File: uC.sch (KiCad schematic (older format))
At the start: 23 parts, among them J4 SWD, SW2 RESET, SW3 BOOT, U9 STM32L073CZTx, Y1 8MHz, Y2 32.768kHz

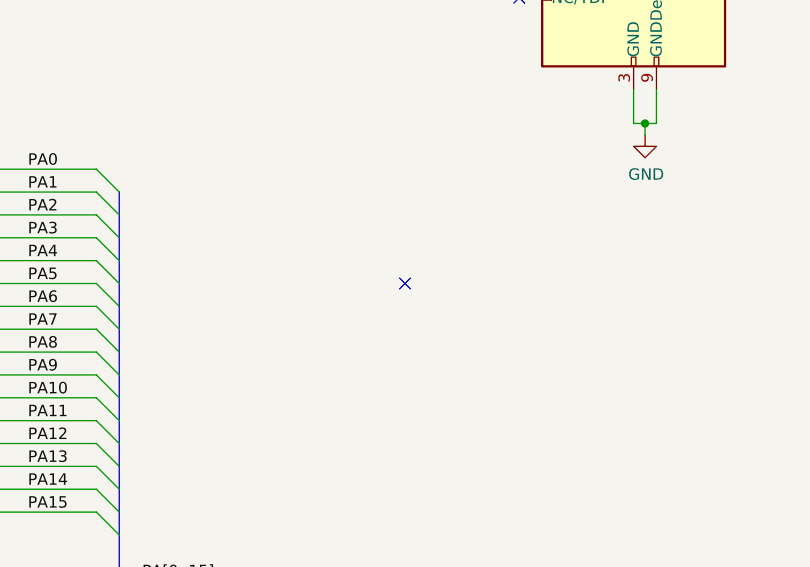
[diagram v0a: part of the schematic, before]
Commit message: Add digikey pn's to schematic, update BOM
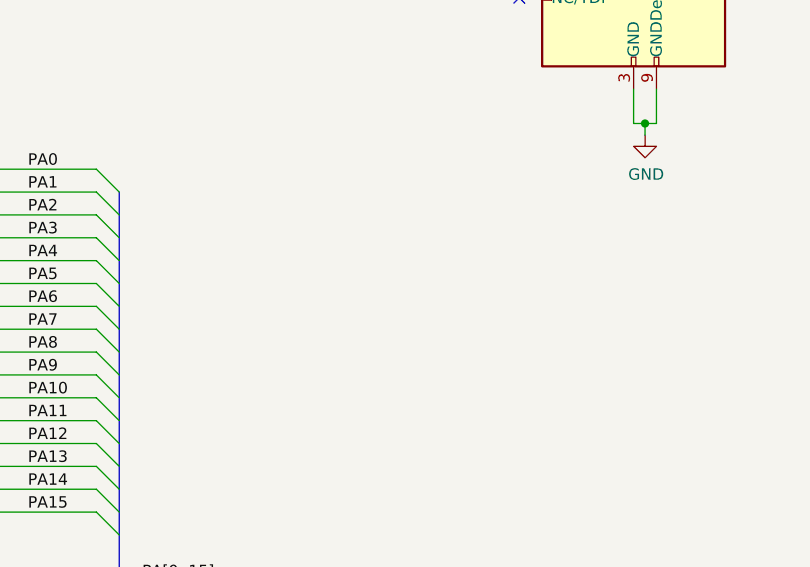
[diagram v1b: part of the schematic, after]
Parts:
- C18, C19, C20, C25, C28: Digikey (none) -> 490-14603-1-ND
- C21, C23, L4: Digikey (none) -> 587-1932-1-ND
- C22: Digikey (none) -> 311-1439-1-ND
- C24, C26: Digikey (none) -> 311-1666-1-ND
- C27, C29: Digikey (none) -> 311-1017-1-ND
- J4: Digikey (none) -> SAM8796-ND; LCSC (none) -> DNP
- R13, R14: Digikey (none) -> 311-10.0KLRTR-ND
- R15: Digikey (none) -> 311-330LRCT-ND
- SW2, SW3: Digikey (none) -> EG2531CT-ND
- U9: Digikey (none) -> 497-17506-ND; LCSC (none) -> DNP
- Y1: Digikey (none) -> 535-10630-1-ND
- Y2: Digikey (none) -> 535-9542-1-ND
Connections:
- no-connect marks 3 -> 2
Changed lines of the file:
@@
 F 2 "jlcpcb_smt:LQFP-48_7x7mm_P0.5mm" H 5800 2850 50  0001 R CNN
 F 3 "http://www.st.com/st-web-ui/static/active/en/resource/technical/document/datasheet/DM00141036.pdf" H 6400 4250 50  0001 C CNN
-F 4 "" H 6400 4250 50  0001 C CNN "LCSC"
+F 4 "DNP" H 6400 4250 50  0001 C CNN "LCSC"
+F 5 "497-17506-ND" H 6400 4250 50  0001 C CNN "Digikey"
 	1    6400 4250
 	1    0    0    -1
@@
 F 3 "~" H 3200 1150 50  0001 C CNN
 F 4 "C1015" V 3200 1150 50  0001 C CNN "LCSC"
+F 5 "587-1932-1-ND" V 3200 1150 50  0001 C CNN "Digikey"
 	1    3200 1150
 	0    1    -1   0
@@
 F 3 "~" H 800 1450 50  0001 C CNN
 F 4 "C1525" H 800 1450 50  0001 C CNN "LCSC"
+F 5 "490-14603-1-ND" H 800 1450 50  0001 C CNN "Digikey"
 	1    800  1450
 	1    0    0    -1
@@
 F 3 "~" H 2150 1450 50  0001 C CNN
 F 4 "C52923" H 2150 1450 50  0001 C CNN "LCSC"
+F 5 "311-1439-1-ND" H 2150 1450 50  0001 C CNN "Digikey"
 	1    2150 1450
 	1    0    0    -1
@@
 F 3 "~" H 2350 2650 50  0001 C CNN
 F 4 "C25744" H 2350 2650 50  0001 C CNN "LCSC"
+F 5 "311-10.0KLRTR-ND" H 2350 2650 50  0001 C CNN "Digikey"
 	1    2350 2650
 	1    0    0    -1
@@
 F 3 "~" H 2350 3450 50  0001 C CNN
 F 4 "C318884" V 2350 3250 50  0001 C CNN "LCSC"
+F 5 "EG2531CT-ND" V 2350 3250 50  0001 C CNN "Digikey"
 	1    2350 3250
 	0    1    1    0
@@
 F 3 "~" H 3200 2900 50  0001 C CNN
 F 4 "C318884" V 3200 2700 50  0001 C CNN "LCSC"
+F 5 "EG2531CT-ND" V 3200 2700 50  0001 C CNN "Digikey"
 	1    3200 2700
 	0    1    1    0
@@
 F 3 "~" H 3200 3450 50  0001 C CNN
 F 4 "C25744" H 3200 3450 50  0001 C CNN "LCSC"
+F 5 "311-10.0KLRTR-ND" H 3200 3450 50  0001 C CNN "Digikey"
 	1    3200 3450
 	1    0    0    -1
@@
 F 3 "~" H 3900 3700 50  0001 C CNN
 F 4 "C115962" H 3900 3700 50  0001 C CNN "LCSC"
+F 5 "535-10630-1-ND" H 3900 3700 50  0001 C CNN "Digikey"
 	1    3900 3700
 	1    0    0    -1
@@
 F 3 "~" H 3650 3950 50  0001 C CNN
 F 4 "C1570" H 3650 3950 50  0001 C CNN "LCSC"
+F 5 "311-1666-1-ND" H 3650 3950 50  0001 C CNN "Digikey"
 	1    3650 3950
 	1    0    0    -1
@@
 F 3 "~" H 4150 3950 50  0001 C CNN
 F 4 "C1570" H 4150 3950 50  0001 C CNN "LCSC"
+F 5 "311-1666-1-ND" H 4150 3950 50  0001 C CNN "Digikey"
 	1    4150 3950
 	1    0    0    -1
@@
 F 3 "~" H 4650 4200 50  0001 C CNN
 F 4 "C32346" H 4650 4200 50  0001 C CNN "LCSC"
+F 5 "535-9542-1-ND" H 4650 4200 50  0001 C CNN "Digikey"
 	1    4650 4200
 	1    0    0    -1
@@
 F 3 "~" H 4400 4500 50  0001 C CNN
 F 4 "C1548" H 4400 4500 50  0001 C CNN "LCSC"
+F 5 "311-1017-1-ND" H 4400 4500 50  0001 C CNN "Digikey"
 	1    4400 4500
 	1    0    0    -1
@@
 F 3 "~" H 4900 4500 50  0001 C CNN
 F 4 "C1548" H 4900 4500 50  0001 C CNN "LCSC"
+F 5 "311-1017-1-ND" H 4900 4500 50  0001 C CNN "Digikey"
 	1    4900 4500
 	1    0    0    -1
@@
 F 2 "Connector_PinHeader_1.27mm:PinHeader_2x05_P1.27mm_Vertical_SMD" H 9800 3100 50  0001 C CNN
 F 3 "http://infocenter.arm.com/help/topic/com.arm.doc.ddi0314h/DDI0314H_coresight_components_trm.pdf" V 9450 1850 50  0001 C CNN
-F 4 "" H 9800 3100 50  0001 C CNN "LCSC"
+F 4 "DNP" H 9800 3100 50  0001 C CNN "LCSC"
+F 5 "SAM8796-ND" H 9800 3100 50  0001 C CNN "Digikey"
 	1    9800 3100
 	-1   0    0    -1
@@
 F 3 "~" H 4400 3450 50  0001 C CNN
 F 4 "C25104" V 4400 3450 50  0001 C CNN "LCSC"
+F 5 "311-330LRCT-ND" V 4400 3450 50  0001 C CNN "Digikey"
 	1    4400 3450
 	0    1    1    0
@@
 F 3 "~" H 1250 1450 50  0001 C CNN
 F 4 "C1525" H 1250 1450 50  0001 C CNN "LCSC"
+F 5 "490-14603-1-ND" H 1250 1450 50  0001 C CNN "Digikey"
 	1    1250 1450
 	1    0    0    -1
@@
 F 3 "~" H 1700 1450 50  0001 C CNN
 F 4 "C1525" H 1700 1450 50  0001 C CNN "LCSC"
+F 5 "490-14603-1-ND" H 1700 1450 50  0001 C CNN "Digikey"
 	1    1700 1450
 	1    0    0    -1
@@
 F 3 "~" H 4450 1450 50  0001 C CNN
 F 4 "C1525" H 4450 1450 50  0001 C CNN "LCSC"
+F 5 "490-14603-1-ND" H 4450 1450 50  0001 C CNN "Digikey"
 	1    4450 1450
 	1    0    0    -1
@@
 F 3 "~" H 3700 1450 50  0001 C CNN
 F 4 "C1525" H 3700 1450 50  0001 C CNN "LCSC"
+F 5 "490-14603-1-ND" H 3700 1450 50  0001 C CNN "Digikey"
 	1    3700 1450
 	1    0    0    -1
@@
 F 3 "~" H 2000 3250 50  0001 C CNN
 F 4 "C1525" H 2000 3250 50  0001 C CNN "LCSC"
+F 5 "587-1932-1-ND" H 2000 3250 50  0001 C CNN "Digikey"
 	1    2000 3250
 	1    0    0    -1
@@
 F 3 "~" H 2850 3450 50  0001 C CNN
 F 4 "C1525" H 2850 3450 50  0001 C CNN "LCSC"
+F 5 "587-1932-1-ND" H 2850 3450 50  0001 C CNN "Digikey"
 	1    2850 3450
 	1    0    0    -1
 $EndComp
-NoConn ~ 8800 4550
-$Comp
-L Graphic:Logo_Open_Hardware_Small #LOGO?
+$Comp
+L Graphic:Logo_Open_Hardware_Small #LOGO6
 U 1 1 5DD39AB0
 P 10850 6900
-F 0 "#LOGO?" H 10850 7175 50  0001 C CNN
+F 0 "#LOGO6" H 10850 7175 50  0001 C CNN
 F 1 "Logo_Open_Hardware_Small" H 10850 6675 50  0001 C CNN
 F 2 "" H 10850 6900 50  0001 C CNN
@@
 $EndComp
 $Comp
-L Graphic:SYM_Radio_Waves_Large #SYM?
+L Graphic:SYM_Radio_Waves_Large #SYM6
 U 1 1 5DD39AB6
 P 10300 6850
-F 0 "#SYM?" H 10300 7050 50  0001 C CNN
+F 0 "#SYM6" H 10300 7050 50  0001 C CNN
 F 1 "SYM_Radio_Waves_Large" H 10300 6600 50  0001 C CNN
 F 2 "" H 10300 6650 50  0001 C CNN

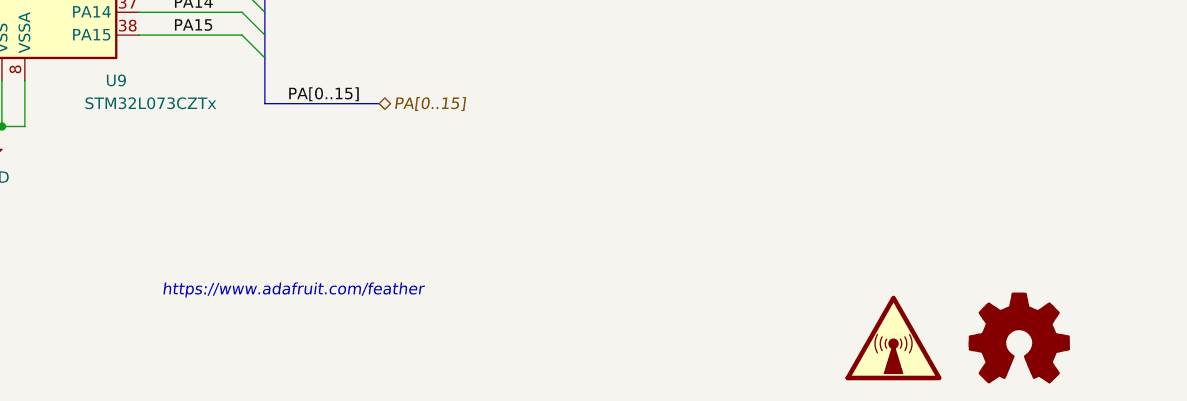
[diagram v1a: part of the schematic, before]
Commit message: PCB REV C0 * Make U8 footprint capable of crypto and fram device * Minor updates to schematic * Minor updates to doc prints * Update bot silk to REV C0
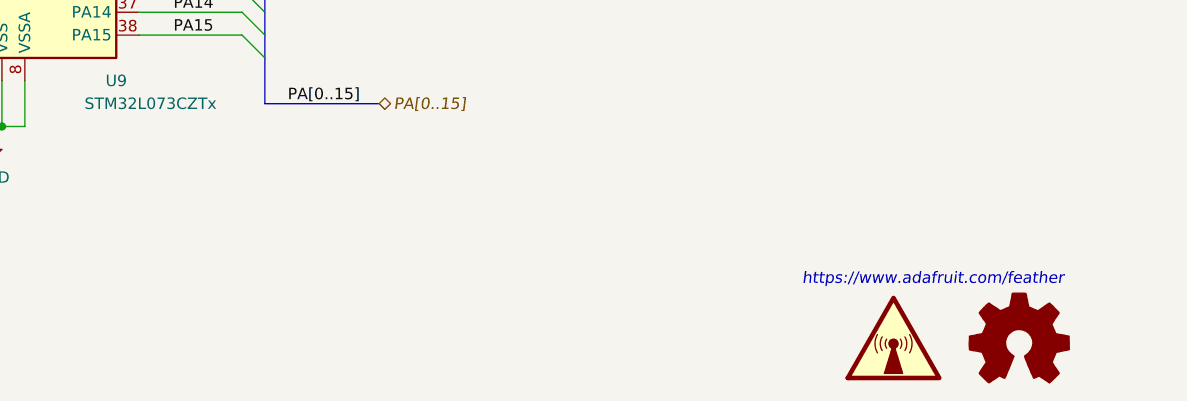
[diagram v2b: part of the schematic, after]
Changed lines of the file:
@@
 EndData
 $EndBitmap
-Text Notes 7100 6700 0    50   Italic 0
+Text Notes 9900 6650 0    50   Italic 0
 https://www.adafruit.com/feather
 $Bitmap
